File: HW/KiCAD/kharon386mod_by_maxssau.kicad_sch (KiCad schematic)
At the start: 0 parts

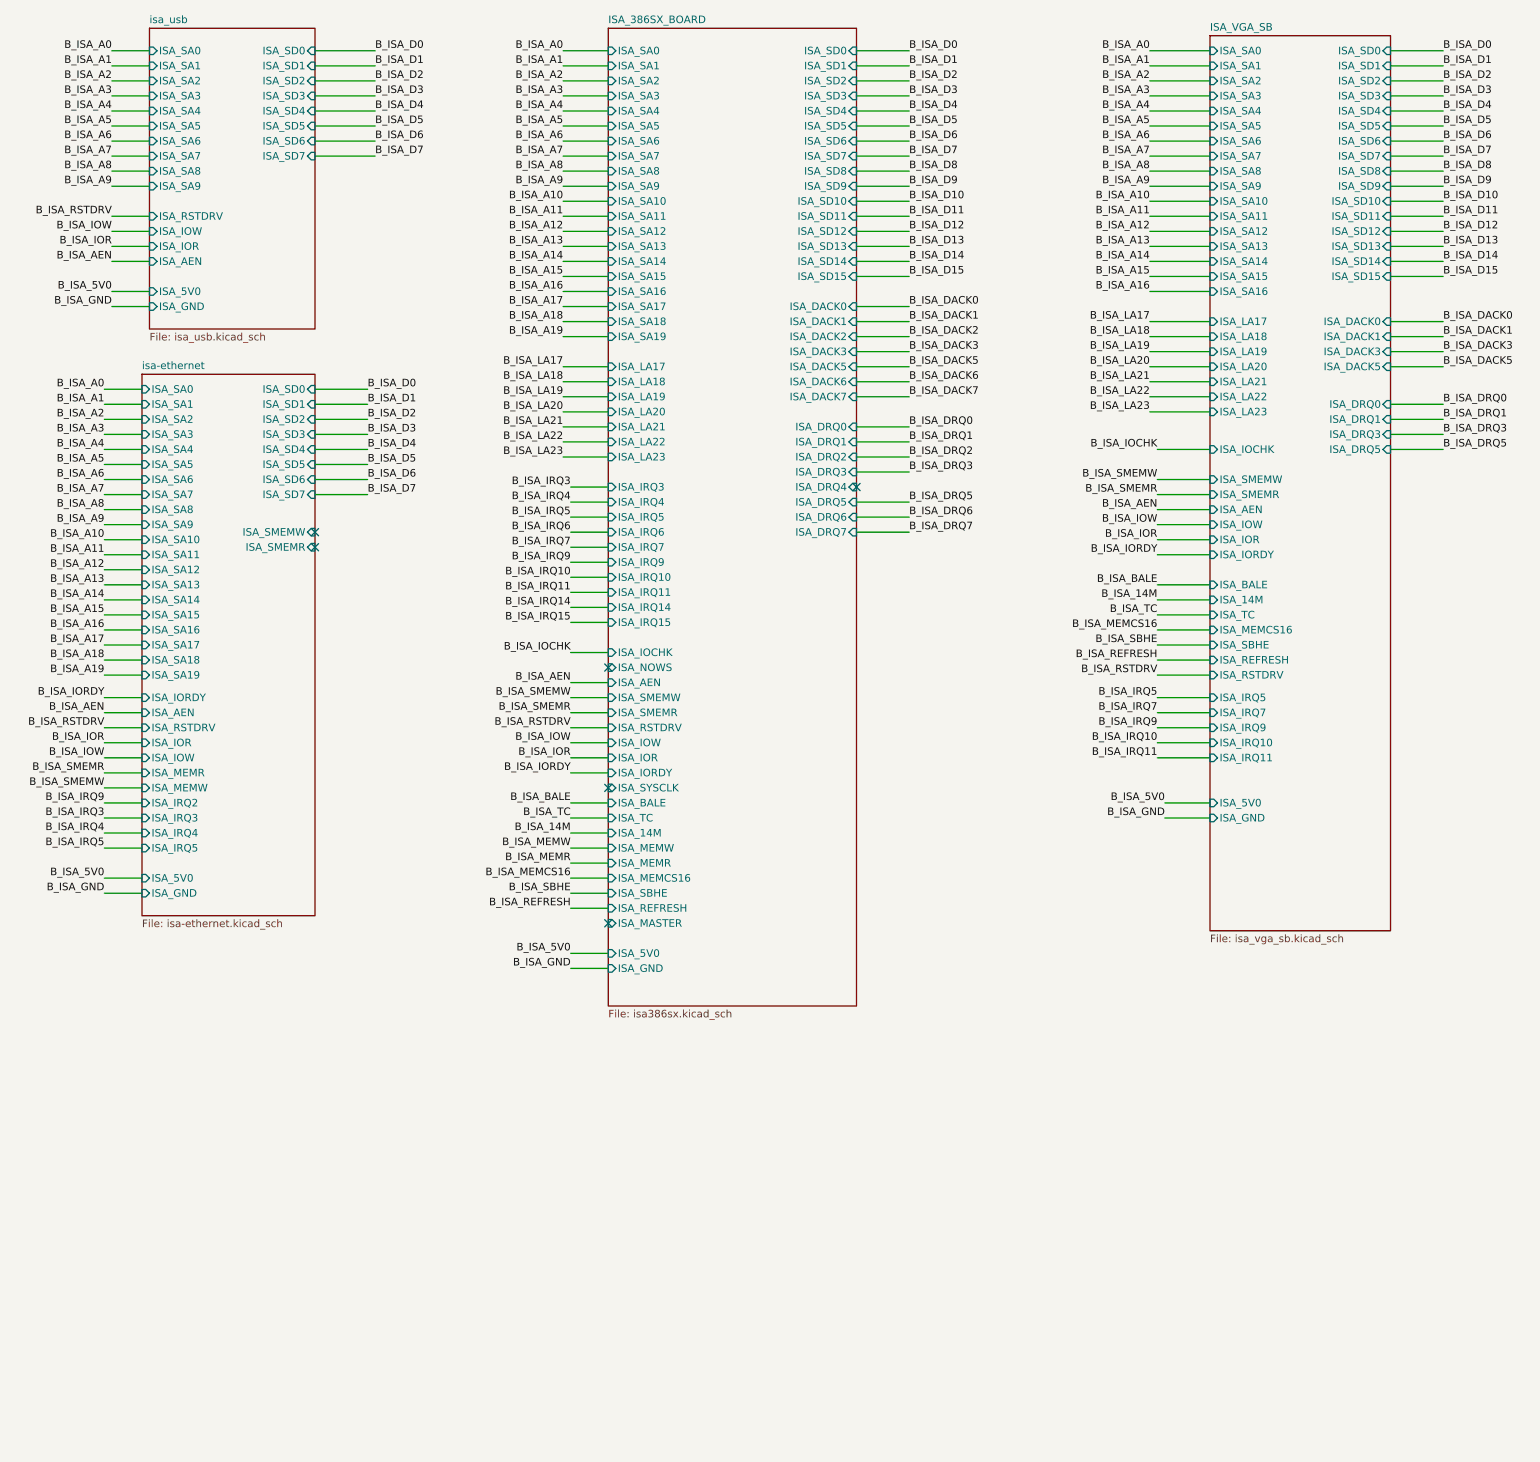
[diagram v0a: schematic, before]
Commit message: some edits, add HP amp
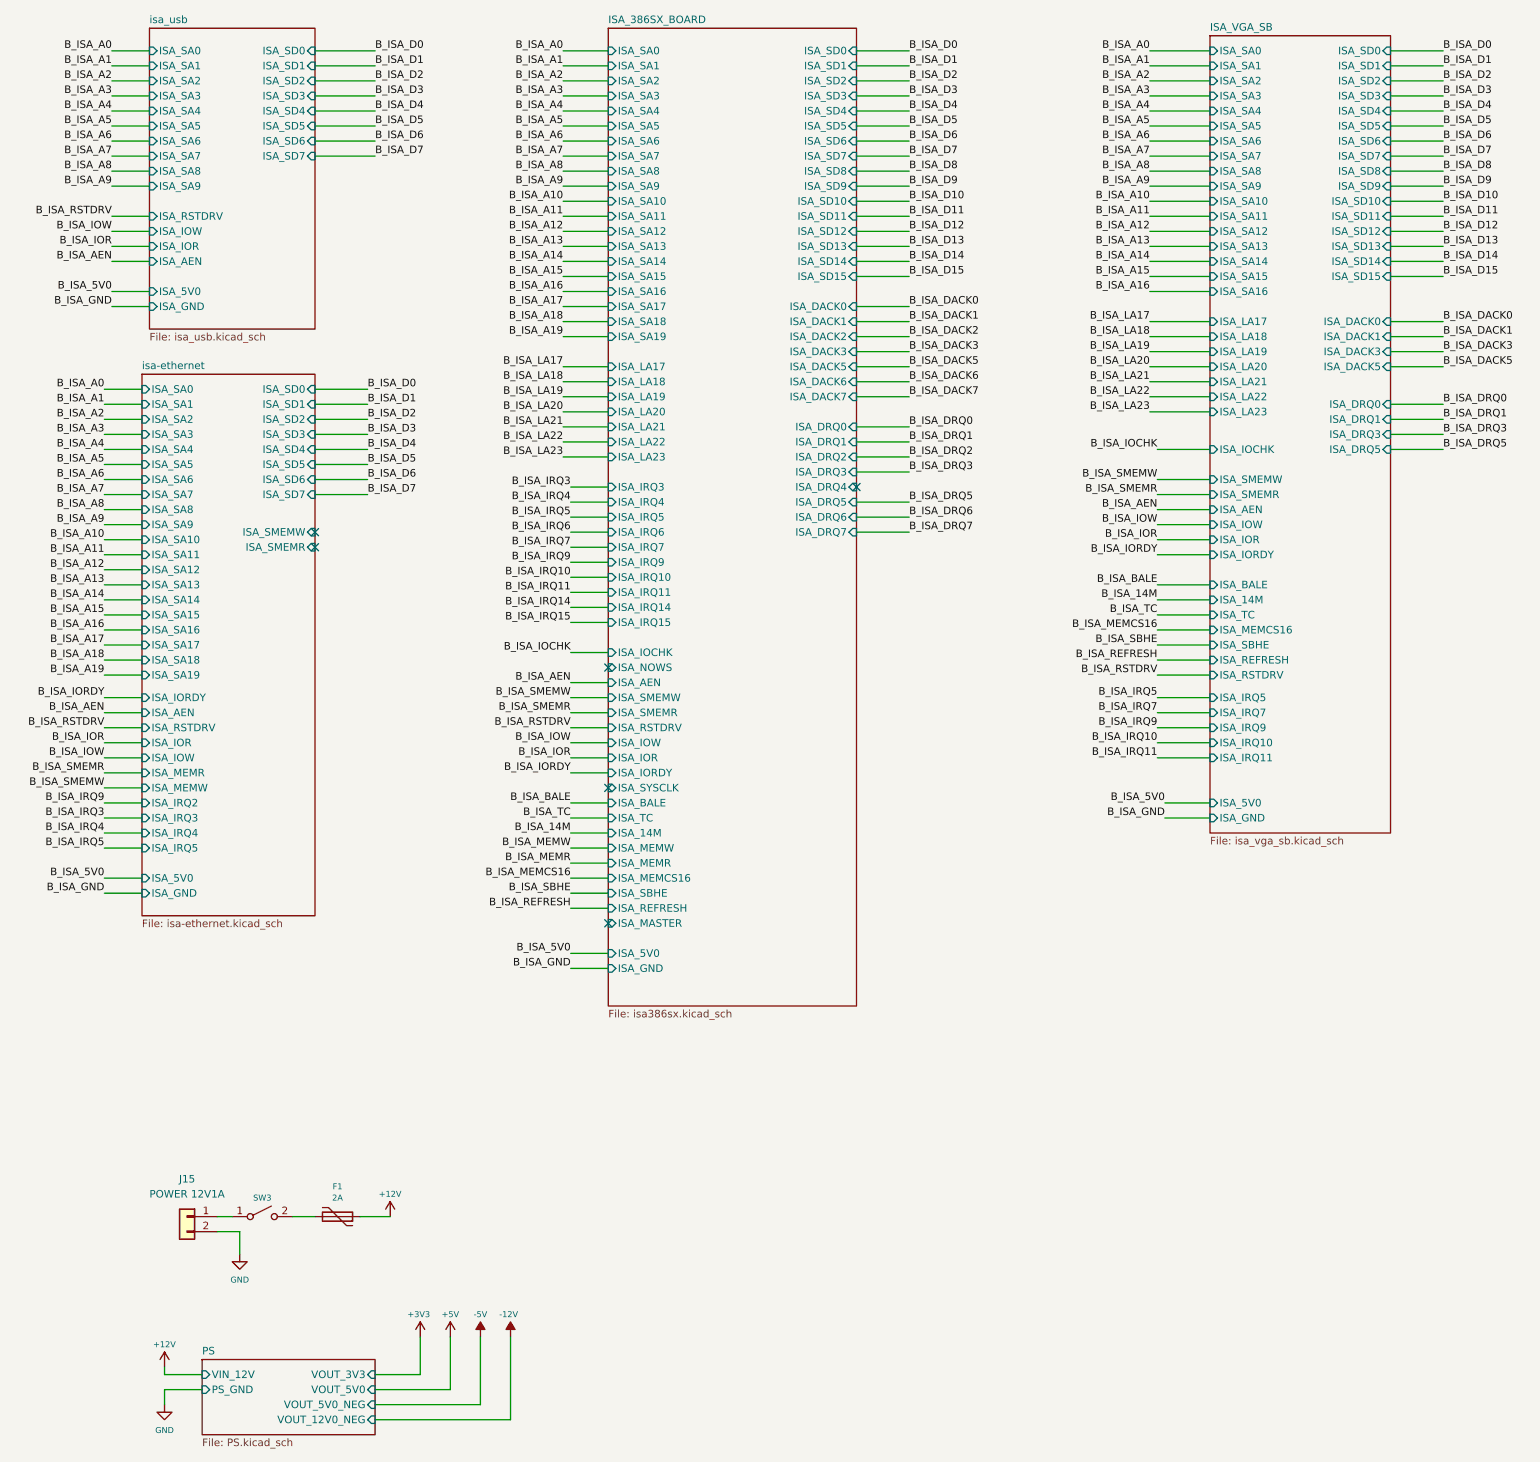
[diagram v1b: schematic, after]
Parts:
- added F1: 2A, Fuse:Fuse_1812_4532Metric_Pad1.30x3.40mm_HandSolder, symbol Device:Polyfuse
- added J15: POWER 12V1A, TerminalBlock:TerminalBlock_bornier-2_P5.08mm, symbol Connector_Generic:Conn_01x02
- added SW3: Jumper / Pin header 1x2 Pitch=2.54mm, Connector_Molex:Molex_KK-254_AE-6410-02A_1x02_P2.54mm_Vertical, symbol Switch:SW_SPST
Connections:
- new net: J15.1 (Pin_1), SW3.1 (A)
- new net: F1.2, SW3.2 (B)
- new net +12V: F1.1
- new net GND: J15.2 (Pin_2)
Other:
- added sheet PS (PS.kicad_sch)
